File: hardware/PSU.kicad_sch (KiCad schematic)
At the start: 29 parts, among them J1 UJ20-C-H-G-SMT-2A-P16-TR, U2 REF35330QDBVR, U4 LM27762, U5 NCP1117-3.3_SOT223

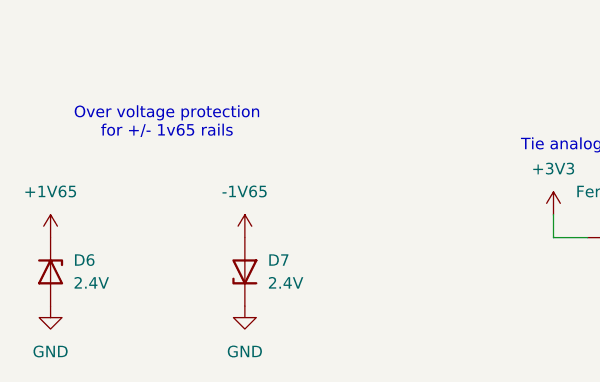
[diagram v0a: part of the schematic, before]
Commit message: docs(hardware): Add offset resistor tolerances to bom
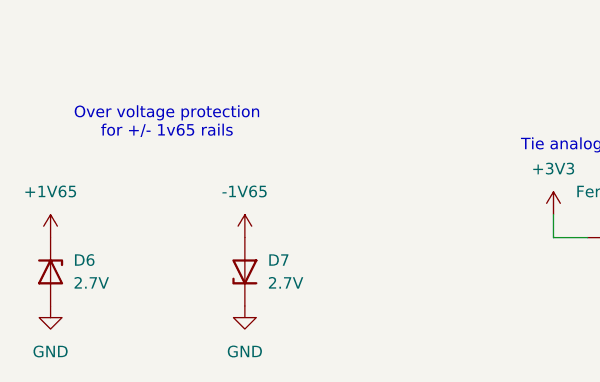
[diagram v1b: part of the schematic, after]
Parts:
- D6, D7: value 2.4V -> 2.7V
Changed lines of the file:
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@@
 			)
 		)
-		(property "Value" "2.4V"
+		(property "Value" "2.7V"
 			(at 69.85 166.3699 90)
 			(effects
@@
 			)
 		)
-		(property "Value" "2.4V"
+		(property "Value" "2.7V"
 			(at 48.26 166.3699 90)
 			(effects
